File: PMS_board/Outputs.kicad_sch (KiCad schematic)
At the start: 27 parts, among them U1 VN7140ASTR, U11 VN7007AHTR, U2 VN7140ASTR, U23 VN7007AHTR, U8 VN7140ASTR

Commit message: Removed nesting in loadwsitching schematic
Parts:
- added C17: 0.1uF, Capacitor_SMD:C_0603_1608Metric, symbol Device:C
- added C18, C5: 0.1uF, Capacitor_SMD:C_0603_1608Metric_Pad1.08x0.95mm_HandSolder, symbol Device:C
- added C19, C26: 100nF, Capacitor_SMD:C_0603_1608Metric, symbol Device:C
- added C24, C28: 100nF, Capacitor_SMD:C_0603_1608Metric_Pad1.08x0.95mm_HandSolder, symbol Device:C
- added C25: 15 uF, Capacitor_SMD:C_0603_1608Metric_Pad1.08x0.95mm_HandSolder, symbol Device:C_Polarized_US
- added C29: 15 uF, Capacitor_SMD:C_0603_1608Metric_Pad1.08x0.95mm_HandSolder, symbol Device:C
- added D26, D27: D_TVS, symbol Device:D_TVS
- added D38: NET_GRN, Diode_SMD:D_0603_1608Metric_Pad1.05x0.95mm_HandSolder, symbol Device:LED
- added D39: BOARD_GRN, Diode_SMD:D_0603_1608Metric_Pad1.05x0.95mm_HandSolder, symbol Device:LED
- added D40: JETSON12V_GRN, Diode_SMD:D_0603_1608Metric_Pad1.05x0.95mm_HandSolder, symbol Device:LED
- added D41: JETSON5V_GRN, Diode_SMD:D_0603_1608Metric_Pad1.05x0.95mm_HandSolder, symbol Device:LED
- added D42: JETSON3V3_GRN, Diode_SMD:D_0603_1608Metric_Pad1.05x0.95mm_HandSolder, symbol Device:LED
- added D6: MOTOR_GRN, Diode_SMD:D_0603_1608Metric_Pad1.05x0.95mm_HandSolder, symbol Device:LED
- added D7: AUX_GRN, Diode_SMD:D_0603_1608Metric_Pad1.05x0.95mm_HandSolder, symbol Device:LED
- added J20: CORE, symbol Connector:Conn_01x02_Pin
- added J21: DRIVE, symbol Connector:Conn_01x02_Pin
- added J22: JET1, symbol Connector:Conn_01x04_Pin
- added J23: JET2, symbol Connector:Conn_01x02_Pin
- added J24: NET, symbol Connector:Conn_01x02_Pin
- added J25: AUX1, symbol Connector:Conn_01x02_Pin
- added J26: AUX2, symbol Connector:Conn_01x02_Pin
- added J27: D1, symbol Connector:Conn_01x02_Pin
- added J28: D2, symbol Connector:Conn_01x02_Pin
- added J29: D3, symbol Connector:Conn_01x02_Pin
- added J30: D4, symbol Connector:Conn_01x02_Pin
- added J31: T1, symbol Connector:Conn_01x02_Pin
- added J32: T2, symbol Connector:Conn_01x02_Pin
- added J33: T3, symbol Connector:Conn_01x02_Pin
- added J34: T4, symbol Connector:Conn_01x02_Pin
- added Q12, Q6: NMOS, Package_DFN_QFN:Nordic_AQFN-94-1EP_7x7mm_P0.4mm, symbol Simulation_SPICE:NMOS
- added R100: 10k, Resistor_SMD:R_0603_1608Metric_Pad0.98x0.95mm_HandSolder, symbol Device:R_US
- added R101: 13.7k, Resistor_SMD:R_0603_1608Metric_Pad0.98x0.95mm_HandSolder, symbol Device:R_US
- added R102: 1.33k, Resistor_SMD:R_0603_1608Metric_Pad0.98x0.95mm_HandSolder, symbol Device:R_US
- added R106: 2.15k, Resistor_SMD:R_0603_1608Metric_Pad0.98x0.95mm_HandSolder, symbol Device:R_US
- added R107: 1M, Resistor_SMD:R_0603_1608Metric_Pad0.98x0.95mm_HandSolder, symbol Device:R_US
- added R108: 1, symbol Device:R_US
- added R12, R13, R14, R16: 1k2, Resistor_SMD:R_0603_1608Metric_Pad0.98x0.95mm_HandSolder, symbol Device:R_US
- added R17: 500R, Resistor_SMD:R_0603_1608Metric_Pad0.98x0.95mm_HandSolder, symbol Device:R_US
- added R18: 220R, Resistor_SMD:R_0603_1608Metric_Pad0.98x0.95mm_HandSolder, symbol Device:R_US
- added R22: 100R, Resistor_SMD:R_0603_1608Metric_Pad0.98x0.95mm_HandSolder, symbol Device:R_US
- added R99: 210k, Resistor_SMD:R_0603_1608Metric_Pad0.98x0.95mm_HandSolder, symbol Device:R_US
- added TP10, TP3, TP4, TP8, TP9: TestPoint, symbol Connector:TestPoint
- added U25: TLV7011DCKR, TLV7011DCKR:DCK0005A_N, symbol TLV7011DCKR:TLV7011DCKR
- added U28: LT1910, Package_DFN_QFN:DFN-24-1EP_4x7mm_P0.5mm_EP2.64x6.44mm, symbol MRDT_ICs:LT1910
- added U29: IRFS7530TRL7PP, IRFS7530TRL7PP:PG-TO263-7_INF, symbol IRFS7530TRL7PP:IRFS7530TRL7PP
- added U30, U31: LM74700, Package_TO_SOT_SMD:SOT-23-6, symbol Power_Management:LM74700
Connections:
- net +24V: now also C5.2, U28.6 (SENSE), U28.8 (V+)
- net +3V3: now also J22.2 (Pin_2), R106.2, U25.5 (V+)
- net Aux_Power1: now also C19.1, C24.1, D26.2 (A2), Q6.3 (S), U30.3 (EN), U30.6 (ANODE)
- net Aux_Power2: now also C25.1, D7.2 (A), J25.2 (Pin_2), J26.2 (Pin_2), Q6.1 (D), TP3.1, U30.4 (CATHODE)
- net Board_Power: now also D39.2 (A), J20.2 (Pin_2), J21.2 (Pin_2), TP8.1
- net Fault_Brakes: now also U28.3 (FAULT)
- net GND: now also C17.1, C17.2, C18.2, C19.2, C25.2, C26.2, C29.2, C5.1, D26.1 (A1), D27.1 (A1), J20.1 (Pin_1), J21.1 (Pin_1), J22.1 (Pin_1), J23.1 (Pin_1), J24.1 (Pin_1), J25.1 (Pin_1), J26.1 (Pin_1), J27.1 (Pin_1), J28.1 (Pin_1), J29.1 (Pin_1), J30.1 (Pin_1), J31.1 (Pin_1), J32.1 (Pin_1), J33.1 (Pin_1), J34.1 (Pin_1), R100.1, R102.2, R108.2, R12.2, R13.2, R14.2, R16.2, R17.2, R18.2, R22.2, U25.2 (V-), U28.1 (GND), U30.2 (GND), U31.2 (GND)
- net Jetson_Power: now also D40.2 (A), J22.4 (Pin_4), J23.2 (Pin_2), TP9.1
- net Motor_Power1: now also C26.1, C28.1, D27.2 (A2), Q12.3 (S), U31.3 (EN), U31.6 (ANODE)
- net Motor_Power2: now also C29.1, D6.2 (A), J27.2 (Pin_2), J28.2 (Pin_2), J29.2 (Pin_2), J30.2 (Pin_2), J31.2 (Pin_2), J32.2 (Pin_2), J33.2 (Pin_2), J34.2 (Pin_2), Q12.1 (D), R99.2, TP4.1, U29.2 (S), U29.3 (S), U29.4 (S), U29.5 (S), U29.6 (S), U31.4 (CATHODE)
- net Network_Power: now also D38.2 (A), J24.2 (Pin_2), TP10.1
- new net: D7.1 (K), R13.1
- new net: C18.1, U28.2 (TIMER)
- new net: R107.2, U25.1 (OUT), U28.4 (IN)
- new net: U28.5 (GATE), U29.1 (G)
- new net: R108.1, U29.7 (D)
- new net: R100.2, R101.1, R99.1
- new net: R101.2, R107.1, U25.3 (IN+)
- new net: R102.1, R106.1, U25.4 (IN-)
- new net: D38.1 (K), R14.1
- new net: D40.1 (K), R17.1
- new net: C24.2, U30.1 (VCAP)
- new net: Q6.2 (G), U30.5 (GATE)
- new net: D6.1 (K), R12.1
- new net: D39.1 (K), R16.1
- new net: C28.2, U31.1 (VCAP)
- new net: D41.1 (K), R18.1
- new net: Q12.2 (G), U31.5 (GATE)
- new net: D42.1 (K), R22.1
- new net +3V3 (Jetson): D42.2 (A)
- new net +5V: D41.2 (A), J22.3 (Pin_3)
- no-connect marks 0 -> 1
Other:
- removed sheet Indicator LEDs
- removed sheet Output Rails
- removed sheet Reverse Voltage & Brake Chopper
- note added: "Aux Ideal Diode"
- note added: "Brake Chopper"
- note added: "Motor Ideal Diode"
- moved on the sheet: C54, C59, D12, D20, D22, R19, R20, R67, R68, R69, R70, R71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

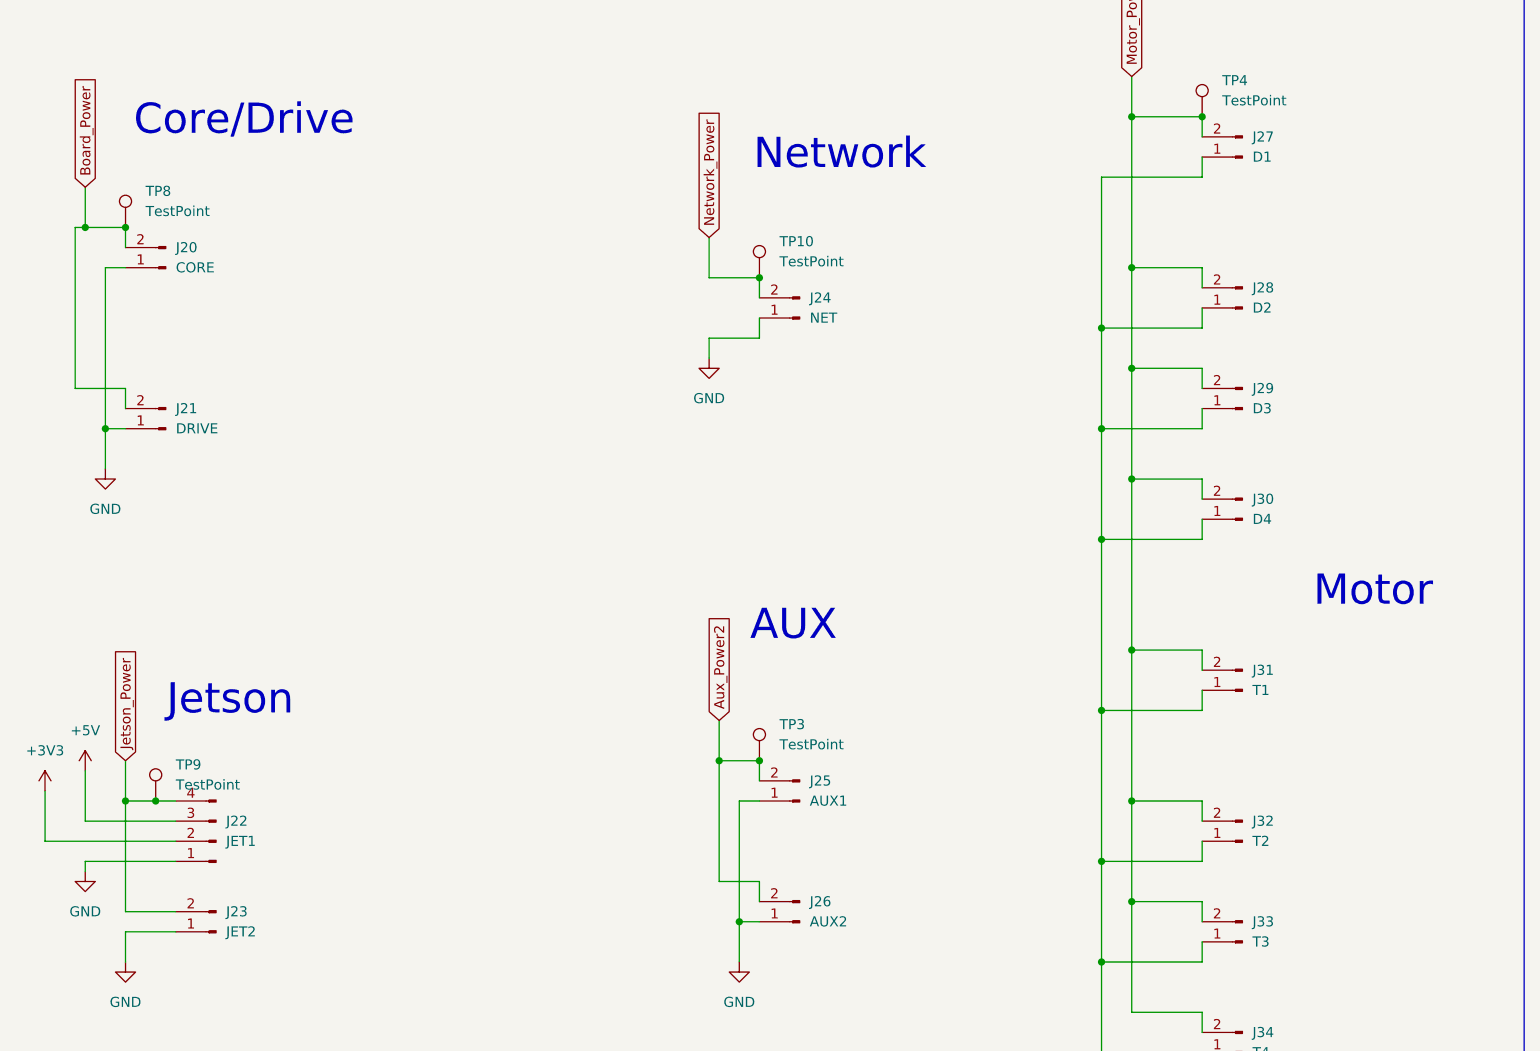
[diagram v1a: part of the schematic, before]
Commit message: Added current budgets for each output rail
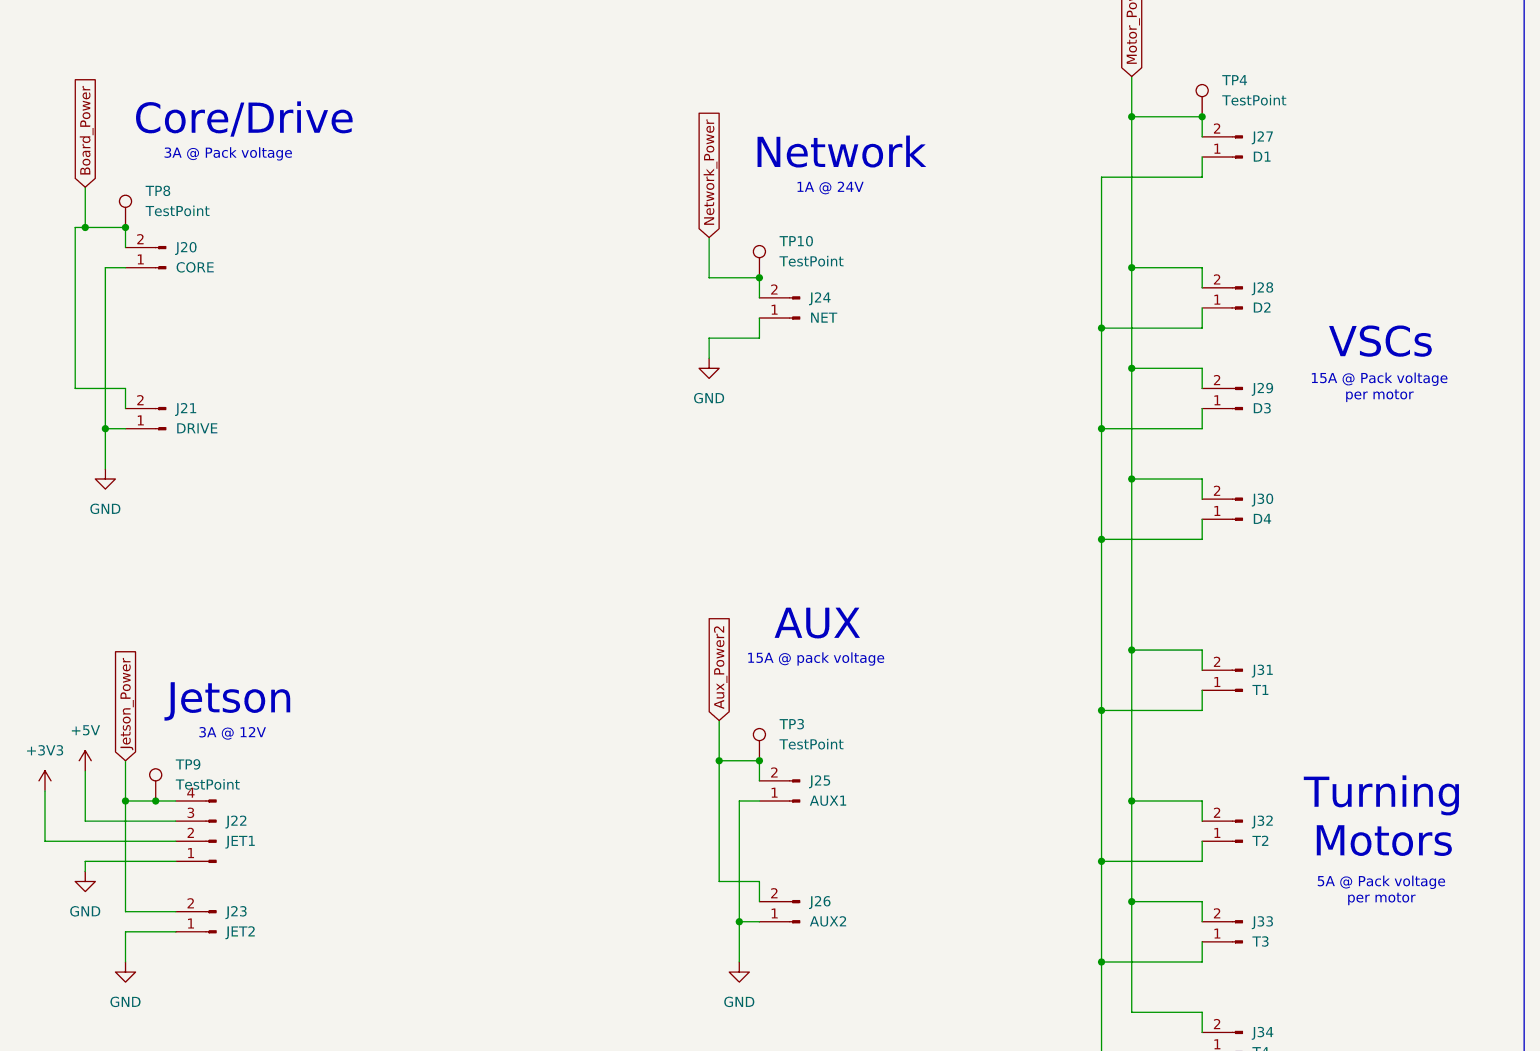
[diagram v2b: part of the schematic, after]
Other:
- note added: "15A @ Pack voltage per motor"
- note added: "15A @ pack voltage"
- note added: "1A @ 24V"
- note added: "3A @ 12V"
- note added: "3A @ Pack voltage"
- note added: "5A @ Pack voltage per motor"
- note added: "Turning Motors"
- note added: "VSCs"
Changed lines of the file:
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@@
+		)
+	)
+	(text "15A @ Pack voltage\nper motor"
+		(exclude_from_sim no)
+		(at 563.372 107.95 0)
+		(effects
+			(font
+				(size 1.27 1.27)
+			)
 		)
 	)
@@
 	(text "AUX"
 		(exclude_from_sim no)
-		(at 489.458 137.922 0)
+		(at 492.506 137.922 0)
 		(effects
 			(font
@@
 		)
 	)
+	(text "Turning\nMotors\n"
+		(exclude_from_sim no)
+		(at 563.88 162.306 0)
+		(effects
+			(font
+				(size 3.81 3.81)
+			)
+		)
+	)
+	(text "3A @ 12V"
+		(exclude_from_sim no)
+		(at 418.592 151.638 0)
+		(effects
+			(font
+				(size 1.27 1.27)
+			)
+		)
+	)
 	(text "AUX"
 		(exclude_from_sim no)
@@
 			(font
 				(size 3.81 3.81)
+			)
+		)
+	)
+	(text "3A @ Pack voltage"
+		(exclude_from_sim no)
+		(at 418.084 78.486 0)
+		(effects
+			(font
+				(size 1.27 1.27)
 			)
 		)
@@
 		)
 	)
-	(text "Motor"
+	(text "1A @ 24V"
 		(exclude_from_sim no)
-		(at 562.61 133.604 0)
+		(at 494.03 82.804 0)
+		(effects
+			(font
+				(size 1.27 1.27)
+			)
+		)
+	)
+	(text "VSCs"
+		(exclude_from_sim no)
+		(at 563.626 102.362 0)
 		(effects
 			(font
@@
 			)
 		)
+	)
+	(text "5A @ Pack voltage\nper motor\n"
+		(exclude_from_sim no)
+		(at 563.626 171.45 0)
+		(effects
+			(font
+				(size 1.27 1.27)
+			)
+		)
+	)
+	(text "15A @ pack voltage"
+		(exclude_from_sim no)
+		(at 492.252 142.24 0)
+		(effects
+			(font
+				(size 1.27 1.27)
+			)
+		)

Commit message: buzzer component
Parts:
- added J1: Chopper_Shunt, LED_THT:LED_D5.0mm_IRGrey, symbol Connector:Conn_01x02_Pin
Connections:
- net GND: now also J1.1 (Pin_1); no longer R108.2
- net at R108.1: no longer U29.7 (D)
- new net: J1.2 (Pin_2), U29.7 (D)
- no-connect marks 1 -> 3
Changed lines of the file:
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@@
 	)
 	(no_connect
+		(at 353.06 163.83)
+	)
+	(no_connect
+		(at 360.68 163.83)
+	)
+	(no_connect
 		(at 347.98 185.42)
 	)
@@
 	(wire
 		(pts
-			(xy 365.76 182.88) (xy 363.22 182.88)
-		)
-		(stroke
-			(width 0)
-			(type default)
-		)
-	)
-	(wire
-		(pts
 			(xy 267.97 181.61) (xy 264.16 181.61)
 		)
@@
 	(wire
 		(pts
+			(xy 355.6 182.88) (xy 360.68 182.88)
+		)
+		(stroke
+			(width 0)
+			(type default)
+		)
+	)
+	(wire
+		(pts
 			(xy 240.03 151.13) (xy 241.3 151.13)
 		)
@@
 	(wire
 		(pts
+			(xy 353.06 182.88) (xy 353.06 181.61)
+		)
+		(stroke
+			(width 0)
+			(type default)
+		)
+	)
+	(wire
+		(pts
 			(xy 86.36 53.34) (xy 87.63 53.34)
 		)
@@
 	(wire
 		(pts
+			(xy 355.6 181.61) (xy 355.6 182.88)
+		)
+		(stroke
+			(width 0)
+			(type default)
+		)
+	)
+	(wire
+		(pts
 			(xy 48.26 116.84) (xy 81.28 116.84)
 		)
@@
 	(wire
 		(pts
-			(xy 365.76 185.42) (xy 365.76 182.88)
+			(xy 360.68 185.42) (xy 360.68 182.88)
 		)
 		(stroke
@@
 	(wire
 		(pts
-			(xy 347.98 182.88) (xy 355.6 182.88)
+			(xy 347.98 182.88) (xy 353.06 182.88)
 		)
 		(stroke
@@
 	(symbol
 		(lib_id "power:GND")
-		(at 365.76 185.42 0)
+		(at 360.68 185.42 0)
 		(unit 1)
 		(body_style 1)
@@
 		(fields_autoplaced yes)
 		(property "Reference" "#PWR0140"
-			(at 365.76 191.77 0)
+			(at 360.68 191.77 0)
 			(hide yes)
 			(show_name no)
@@
 		)
 		(property "Value" "GND"
-			(at 365.76 190.5 0)
+			(at 360.68 190.5 0)
 			(show_name no)
 			(do_not_autoplace no)
@@
 		)
 		(property "Footprint" ""
-			(at 365.76 185.42 0)
+			(at 360.68 185.42 0)
 			(hide yes)
 			(show_name no)
@@
 		)
 		(property "Datasheet" ""
-			(at 365.76 185.42 0)
+			(at 360.68 185.42 0)
 			(hide yes)
 			(show_name no)
@@
 		)
 		(property "Description" "Power symbol creates a global label with name \"GND\" , ground"
-			(at 365.76 185.42 0)
+			(at 360.68 185.42 0)
 			(hide yes)
 			(show_name no)
@@
 	(symbol
 		(lib_id "Device:R_US")
-		(at 359.41 182.88 90)
-		(mirror x)
-		(unit 1)
-		(body_style 1)
-		(exclude_from_sim no)
-		(in_bom yes)
-		(on_board yes)
-		(in_pos_files yes)
-		(dnp no)
-		(property "Reference" "R108"
-			(at 361.442 185.166 90)
-			(show_name no)
-			(do_not_autoplace no)
-			(effects
-				(font
-					(size 1.27 1.27)
-				)
-				(justify left)
-			)
-		)
-		(property "Value" "1"
-			(at 359.918 179.832 90)
-			(show_name no)
-			(do_not_autoplace no)
-			(effects
-				(font
-					(size 1.27 1.27)
-				)
-				(justify left)
-			)
-		)
-		(property "Footprint" ""
-			(at 359.664 183.896 90)
-			(hide yes)
-			(show_name no)
-			(do_not_autoplace no)
-			(effects
-				(font
-					(size 1.27 1.27)
-				)
-			)
-		)
-		(property "Datasheet" ""
-			(at 359.41 182.88 0)
-			(hide yes)
-			(show_name no)
-			(do_not_autoplace no)
-			(effects
-				(font
-					(size 1.27 1.27)
-				)
-			)
-		)
-		(property "Description" "Resistor, US symbol"
-			(at 359.41 182.88 0)
-			(hide yes)
-			(show_name no)
-			(do_not_autoplace no)
-			(effects
-				(font
-					(size 1.27 1.27)
-				)
-			)
-		)
-		(property "KLC_S3.1" ""
-			(at 359.41 182.88 90)
-			(hide yes)
-			(show_name no)
-			(do_not_autoplace no)
-			(effects
-				(font
-					(size 1.27 1.27)
-				)
-			)
-		)
-		(property "KLC_S4.1" ""
-			(at 359.41 182.88 90)
-			(hide yes)
-			(show_name no)
-			(do_not_autoplace no)
-			(effects
-				(font
-					(size 1.27 1.27)
-				)
-			)
-		)
-		(property "KLC_S6.2" ""
-			(at 359.41 182.88 90)
-			(hide yes)
-			(show_name no)
-			(do_not_autoplace no)
-			(effects
-				(font
-					(size 1.27 1.27)
-				)
-			)
-		)
-		(pin "2"
-		)
-		(pin "1"
-		)
-		(instances
-			(project "PMS_board"
-				(path "/282246b0-e0d8-4997-b3ee-58bf10355d52/266cb597-81f7-4ea7-87c1-e1b826fc674e"
-					(reference "R108")
-					(unit 1)
-				)
-			)
-		)
-	)
-	(symbol
-		(lib_id "Device:R_US")
 		(at 76.2 111.76 90)
 		(mirror x)
@@
 	(symbol
 		(lib_id "Device:R_US")
+		(at 356.87 163.83 90)
+		(mirror x)
+		(unit 1)
+		(body_style 1)
+		(exclude_from_sim no)
+		(in_bom yes)
+		(on_board no)
+		(in_pos_files no)
+		(dnp no)
+		(property "Reference" "R108"
+			(at 358.902 166.116 90)
+			(show_name no)
+			(do_not_autoplace no)
+			(effects
+				(font
+					(size 1.27 1.27)
+				)
+				(justify left)
+			)
+		)
+		(property "Value" "1"
+			(at 357.378 160.782 90)
+			(show_name no)
+			(do_not_autoplace no)
+			(effects
+				(font
+					(size 1.27 1.27)
+				)
+				(justify left)
+			)
+		)
+		(property "Footprint" ""
+			(at 357.124 164.846 90)
+			(hide yes)
+			(show_name no)
+			(do_not_autoplace no)
+			(effects
+				(font
+					(size 1.27 1.27)
+				)
+			)
+		)
+		(property "Datasheet" ""
+			(at 356.87 163.83 0)
+			(hide yes)
+			(show_name no)
+			(do_not_autoplace no)
+			(effects
+				(font
+					(size 1.27 1.27)
+				)
+			)
+		)
+		(property "Description" "Resistor, US symbol"
+			(at 356.87 163.83 0)
+			(hide yes)
+			(show_name no)
+			(do_not_autoplace no)
+			(effects
+				(font
+					(size 1.27 1.27)
+				)
+			)
+		)
+		(property "KLC_S3.1" ""
+			(at 356.87 163.83 90)
+			(hide yes)
+			(show_name no)
+			(do_not_autoplace no)
+			(effects
+				(font
+					(size 1.27 1.27)
+				)
+			)
+		)
+		(property "KLC_S4.1" ""
+			(at 356.87 163.83 90)
+			(hide yes)
+			(show_name no)
+			(do_not_autoplace no)
+			(effects
+				(font
+					(size 1.27 1.27)
+				)
+			)
+		)
+		(property "KLC_S6.2" ""
+			(at 356.87 163.83 90)
+			(hide yes)
+			(show_name no)
+			(do_not_autoplace no)
+			(effects
+				(font
+					(size 1.27 1.27)
+				)
+			)
+		)
+		(pin "2"
+		)
+		(pin "1"
+		)
+		(instances
+			(project "PMS_board"
+				(path "/282246b0-e0d8-4997-b3ee-58bf10355d52/266cb597-81f7-4ea7-87c1-e1b826fc674e"
+					(reference "R108")
+					(unit 1)
+				)
+			)
+		)
+	)
+	(symbol
+		(lib_id "Device:R_US")
 		(at 256.54 87.63 0)
 		(unit 1)
@@
 					(unit 1)
 				)
+			)
+		)
+	)
+	(symbol
+		(lib_id "Connector:Conn_01x02_Pin")
+		(at 355.6 176.53 270)
+		(unit 1)
+		(body_style 1)
+		(exclude_from_sim no)
+		(in_bom yes)
+		(on_board yes)
+		(in_pos_files yes)
+		(dnp no)
+		(fields_autoplaced yes)
+		(property "Reference" "J1"
+			(at 356.87 175.8949 90)
+			(show_name no)
+			(do_not_autoplace no)
+			(effects
+				(font
+					(size 1.27 1.27)
+				)
+				(justify left)
+			)
+		)
+		(property "Value" "Chopper_Shunt"
+			(at 356.87 178.4349 90)
+			(show_name no)
+			(do_not_autoplace no)
+			(effects
+				(font
+					(size 1.27 1.27)
+				)
+				(justify left)
+			)
+		)
+		(property "Footprint" "LED_THT:LED_D5.0mm_IRGrey"
+			(at 355.6 176.53 0)
+			(hide yes)
+			(show_name no)
+			(do_not_autoplace no)
+			(effects
+				(font
+					(size 1.27 1.27)
+				)
+			)
+		)
+		(property "Datasheet" ""
+			(at 355.6 176.53 0)
+			(hide yes)
+			(show_name no)
+			(do_not_autoplace no)
+			(effects
+				(font
+					(size 1.27 1.27)
+				)
+			)
+		)
+		(property "Description" "Generic connector, single row, 01x02, script generated"
+			(at 355.6 176.53 0)
+			(hide yes)
+			(show_name no)
+			(do_not_autoplace no)
+			(effects
+				(font
+					(size 1.27 1.27)
+				)
+			)
+		)
+		(pin "1"
+		)
+		(pin "2"
+		)
+		(instances
+			(project "PMS_board"
+				(path "/282246b0-e0d8-4997-b3ee-58bf10355d52/266cb597-81f7-4ea7-87c1-e1b826fc674e"
+					(reference "J1")
+					(unit 1)
+				)

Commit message: Fixed some broken footprints
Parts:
- J1: footprint LED_THT:LED_D5.0mm_IRGrey -> (none)
- TP10, TP3, TP4, TP8, TP9: footprint (none) -> TestPoint:TestPoint_Pad_D1.0mm
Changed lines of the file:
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@@
 			)
 		)
-		(property "Footprint" ""
+		(property "Footprint" "TestPoint:TestPoint_Pad_D1.0mm"
 			(at 546.1 73.66 0)
 			(hide yes)
@@
 			)
 		)
-		(property "Footprint" ""
+		(property "Footprint" "TestPoint:TestPoint_Pad_D1.0mm"
 			(at 410.21 87.63 0)
 			(hide yes)
@@
 			)
 		)
-		(property "Footprint" ""
+		(property "Footprint" "TestPoint:TestPoint_Pad_D1.0mm"
 			(at 490.22 93.98 0)
 			(hide yes)
@@
 			)
 		)
-		(property "Footprint" "LED_THT:LED_D5.0mm_IRGrey"
+		(property "Footprint" ""
 			(at 355.6 176.53 0)
 			(hide yes)
@@
 			)
 		)
-		(property "Footprint" ""
+		(property "Footprint" "TestPoint:TestPoint_Pad_D1.0mm"
 			(at 490.22 154.94 0)
 			(hide yes)
@@
 			)
 		)
-		(property "Footprint" ""
+		(property "Footprint" "TestPoint:TestPoint_Pad_D1.0mm"
 			(at 414.02 160.02 0)
 			(hide yes)

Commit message: Zener Footprints
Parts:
- D12, D20, D22: footprint (none) -> MRDT_Passives:SOT-23_Diode
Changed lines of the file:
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@@
 			)
 		)
-		(property "Footprint" ""
+		(property "Footprint" "MRDT_Passives:SOT-23_Diode"
 			(at 67.31 160.02 0)
 			(hide yes)
@@
 			)
 		)
-		(property "Footprint" ""
+		(property "Footprint" "MRDT_Passives:SOT-23_Diode"
 			(at 67.31 124.46 0)
 			(hide yes)
@@
 			)
 		)
-		(property "Footprint" ""
+		(property "Footprint" "MRDT_Passives:SOT-23_Diode"
 			(at 67.31 195.58 0)
 			(hide yes)
